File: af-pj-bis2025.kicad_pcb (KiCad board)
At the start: 2 copper layers, 70 x 88.8 mm, 81 parts, among them J1 CN7, J2 CN10, J3 Conn_01x06, J4 Conn_Coaxial, J5 Barrel_Jack_MountingPin, J7 Conn_Coaxial, J8 Conn_01x10, U1 MIC5237-5.0YU, U2 ALD114904APAL, U3 OPA2380AIDGKR, U4 THS4552IPWR, U5 REF5050IDR, U6 LT1991ACMS-TRPBF, U7 UA78L06ACPK, U8 ADS1220IPW

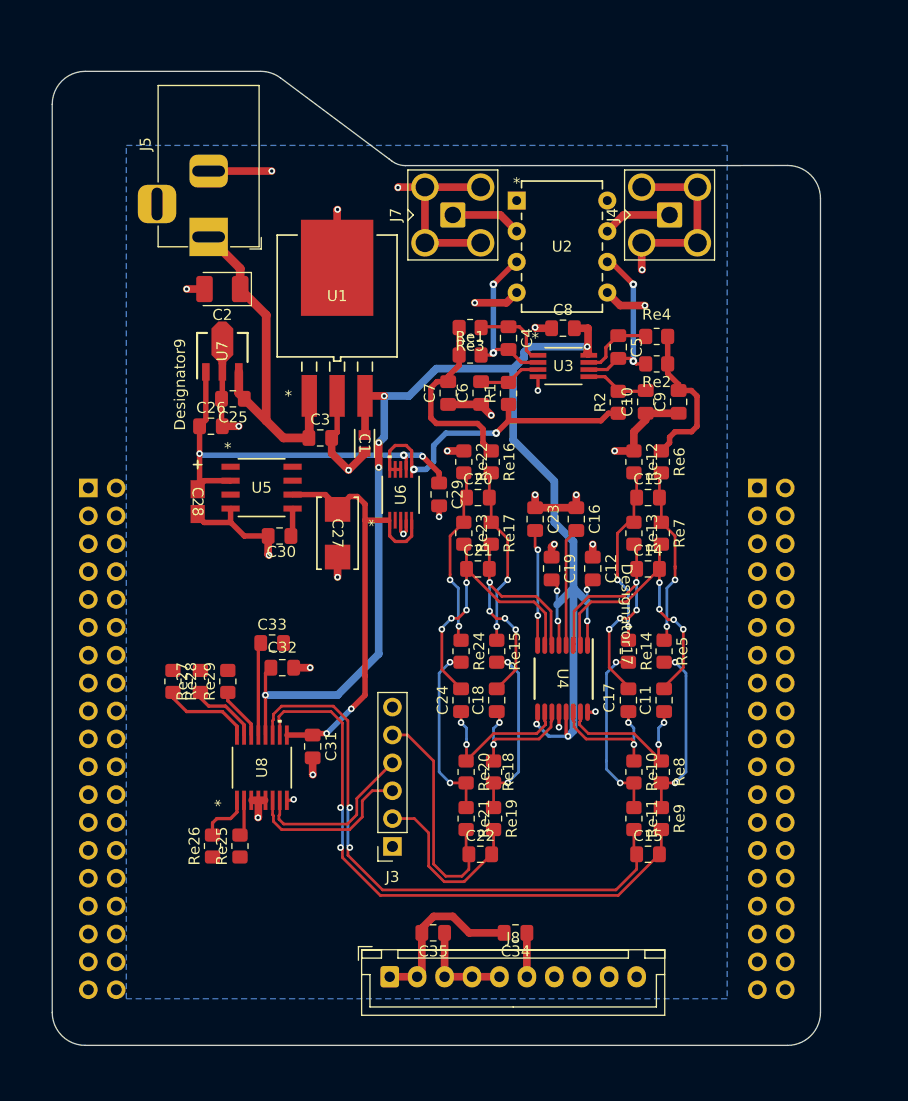
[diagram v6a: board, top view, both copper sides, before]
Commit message: DRC,LVSクリアとテストピン、デバック用ピン追加
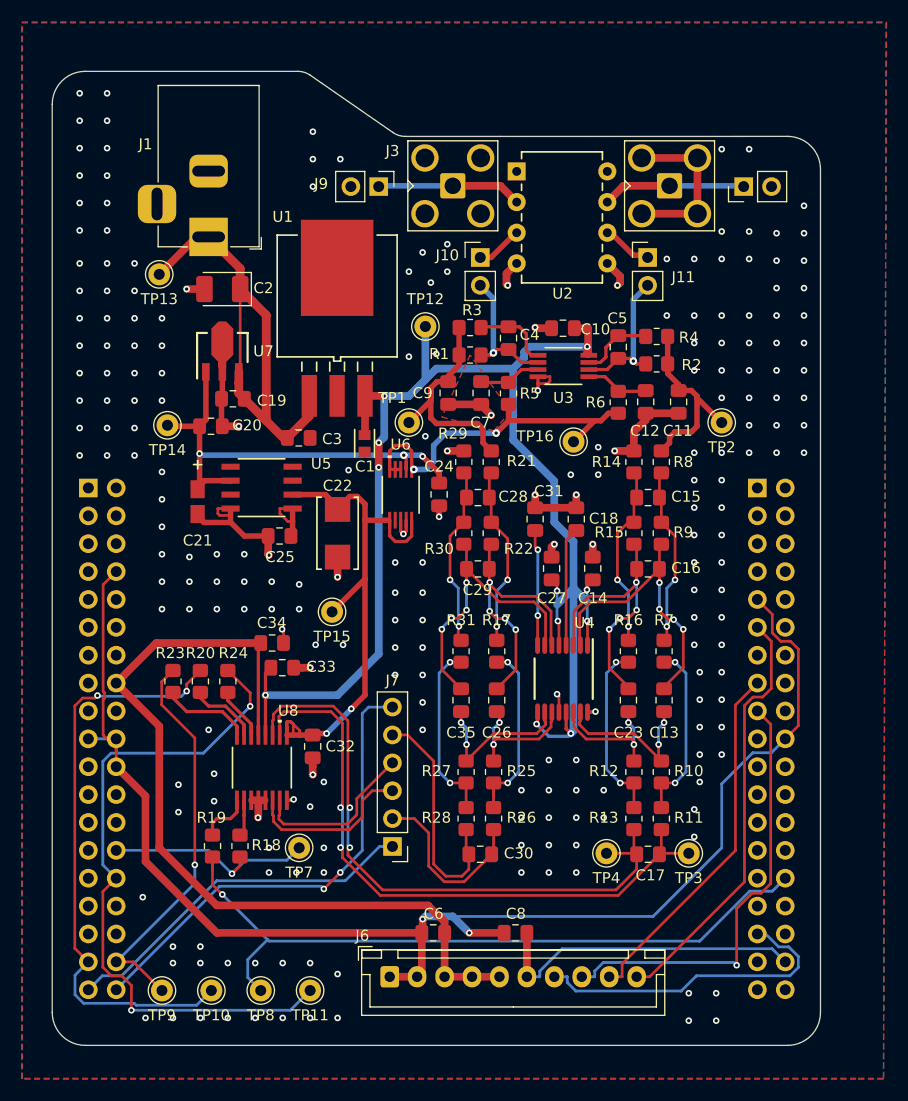
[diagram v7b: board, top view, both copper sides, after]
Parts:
- removed the J1 at (149.8, 88.2)
- removed the J3 at (177.5, 120.9)
- added J10: Conn_01x02, Connector_PinHeader_2.54mm:PinHeader_1x02_P2.54mm_Vertical, F.Cu at (185.5, 67.2)
- added J11: Conn_01x02, Connector_PinHeader_2.54mm:PinHeader_1x02_P2.54mm_Vertical, F.Cu at (200.8, 67.2)
- added J5: CN10, Connector_PinSocket_2.54mm:PinSocket_2x19_P2.54mm_Vertical, B.Cu at (210.8, 88.2)
- added J7: Conn_01x06, Connector_PinHeader_2.54mm:PinHeader_1x06_P2.54mm_Vertical, F.Cu at (177.5, 120.9)
- added J8: Conn_01x02, Connector_PinHeader_2.54mm:PinHeader_1x02_P2.54mm_Vertical, F.Cu at (209.5, 60.8)
- added J9: Conn_01x02, Connector_PinHeader_2.54mm:PinHeader_1x02_P2.54mm_Vertical, F.Cu at (176.2, 60.8)
- added TP1: TestPoint, Connector_Pin:Pin_D1.0mm_L10.0mm, F.Cu at (179.0, 82.2)
- added TP10: TestPoint, Connector_Pin:Pin_D1.0mm_L10.0mm, F.Cu at (161.0, 134.0)
- added TP11: TestPoint, Connector_Pin:Pin_D1.0mm_L10.0mm, F.Cu at (170.0, 134.0)
- added TP12: TestPoint, Connector_Pin:Pin_D1.0mm_L10.0mm, F.Cu at (180.5, 73.5)
- added TP13: TestPoint, Connector_Pin:Pin_D1.0mm_L10.0mm, F.Cu at (156.2, 68.8)
- added TP14: TestPoint, Connector_Pin:Pin_D1.0mm_L10.0mm, F.Cu at (157.0, 82.5)
- added TP15: TestPoint, Connector_Pin:Pin_D1.0mm_L10.0mm, F.Cu at (172.0, 99.5)
- added TP16: TestPoint, Connector_Pin:Pin_D1.0mm_L10.0mm, F.Cu at (194.0, 84.0)
- added TP2: TestPoint, Connector_Pin:Pin_D1.0mm_L10.0mm, F.Cu at (207.5, 82.2)
- added TP3: TestPoint, Connector_Pin:Pin_D1.0mm_L10.0mm, F.Cu at (204.5, 121.5)
- added TP4: TestPoint, Connector_Pin:Pin_D1.0mm_L10.0mm, F.Cu at (197.0, 121.5)
- added TP7: TestPoint, Connector_Pin:Pin_D1.0mm_L10.0mm, F.Cu at (169.0, 121.0)
- added TP8: TestPoint, Connector_Pin:Pin_D1.0mm_L10.0mm, F.Cu at (165.5, 134.0)
- added TP9: TestPoint, Connector_Pin:Pin_D1.0mm_L10.0mm, F.Cu at (156.5, 134.0)
- J2: value CN10 -> CN7
- moved J2 61.0 mm to (149.8, 88.2)
- moved J3 2.66 mm to (183.0, 60.7)
- moved J4 2.66 mm to (202.8, 60.7)
- moved U2 2.66 mm to (188.8, 59.4)
- moved C3 1.96 mm to (169.0, 83.7)
- renumbered C8 to C10, C9 to C11, C10 to C12, C11 to C13, C12 to C14, C13 to C15, C14 to C16, C15 to C17, C16 to C18, C25 to C19, C26 to C20, C28 to C21, C27 to C22, C17 to C23, C29 to C24, C30 to C25, C18 to C26, C19 to C27, C20 to C28, C21 to C29, C22 to C30, C23 to C31, C31 to C32, C32 to C33, C33 to C34, C24 to C35, C35 to C6, C6 to C7, C34 to C8, C7 to C9, J5 to J1, J7 to J3, J8 to J6, Re1 to R1, Re8 to R10, Re9 to R11, Re10 to R12, Re11 to R13, Re12 to R14, Re13 to R15, Re14 to R16, Re15 to R17, Re25 to R18, Re26 to R19, Re2 to R2, Re27 to R20, Re16 to R21, Re17 to R22, Re28 to R23, Re29 to R24, Re18 to R25, Re19 to R26, Re20 to R27, Re21 to R28, Re22 to R29, Re3 to R3, Re23 to R30, Re24 to R31, Re4 to R4, R1 to R5, R2 to R6, Re5 to R7, Re6 to R8, Re7 to R9
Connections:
- C4 pad 2: Net-(U2-DN1) -> Net-(J10-Pin_2)
- C5 pad 2: Net-(U2-DN2) -> Net-(J11-Pin_2)
- J1 pad 3: (no net) -> /AVSS
- J2 pad 12: unconnected-(J2-Pin_12-Pad12) -> /IOREF
- J2 pad 14: unconnected-(J2-Pin_14-Pad14) -> /~{RST}
- J2 pad 16: unconnected-(J2-Pin_16-Pad16) -> +3V3
- J2 pad 18: unconnected-(J2-Pin_18-Pad18) -> +5V
- J2 pad 19: unconnected-(J2-Pin_19-Pad19) -> GND
- J2 pad 22: unconnected-(J2-Pin_22-Pad22) -> GND
- J2 pad 24: unconnected-(J2-Pin_24-Pad24) -> /VIN
- J2 pad 28: unconnected-(J2-Pin_28-Pad28) -> /ADC_CS
- J2 pad 30: unconnected-(J2-Pin_30-Pad30) -> /ADC_DRDY
- J2 pad 32: GNDA -> unconnected-(J2-Pin_32-Pad32)
- J2 pad 33: unconnected-(J2-Pin_33-Pad33) -> +BATT
- J2 pad 35: unconnected-(J2-Pin_35-Pad35) -> /ADC_MISO
- J2 pad 36: unconnected-(J2-Pin_36-Pad36) -> /ADC_MOSI
- J2 pad 37: unconnected-(J2-Pin_37-Pad37) -> /AIN2_mcuN
- J2 pad 38: unconnected-(J2-Pin_38-Pad38) -> /AIN2_mcuP
- J2 pad 5: unconnected-(J2-Pin_5-Pad5) -> VDD
- J2 pad 6: unconnected-(J2-Pin_6-Pad6) -> /E5V
- J2 pad 8: /5V_USB_CHGR -> GND
- J6 pad 7: /LCD_EXCOMIN -> /LCD_EXTCOMIN
- R1 pad 2: Net-(U2-DN1) -> Net-(J10-Pin_2)
- R2 pad 2: Net-(U2-DN2) -> Net-(J11-Pin_2)
- U2 pad 3: Net-(U2-DN1) -> Net-(J10-Pin_1)
- U2 pad 6: Net-(U2-DN2) -> Net-(J11-Pin_1)
- U3 pad 2: Net-(U2-DN1) -> Net-(J10-Pin_2)
- U3 pad 6: Net-(U2-DN2) -> Net-(J11-Pin_2)
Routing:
- net GND: track 15.7 -> 132.5 mm, vias 0 -> 2
- net /ADC_SCLK: track 0.00 -> 66.3 mm, vias 0 -> 1
- net +3V3: track 17.5 -> 83.6 mm
- net /ADC_DRDY: track 0.00 -> 62.0 mm, vias 0 -> 2
- net /ADC_MISO: track 0.00 -> 53.9 mm, vias 0 -> 2
- net /AIN2_mcuP: track 0.00 -> 43.5 mm, vias 0 -> 2
- net /LCD_CS: track 0.00 -> 40.5 mm, vias 0 -> 1
- net /LCD_SCLK: track 0.00 -> 38.7 mm
- net /ADC_MOSI: track 0.00 -> 36.4 mm, vias 0 -> 1
- net /AVSS: track 123.6 -> 89.6 mm, vias 28 -> 231
- net /AIN2_mcuN: track 0.00 -> 33.7 mm
- net /LCD_MOSI: track 0.00 -> 33.0 mm
- net /LCD_EXTCOMIN: track 0.00 -> 29.5 mm
- net /LCD_DISP: track 4.00 -> 29.4 mm
- net /ADC_CS: track 0.00 -> 20.5 mm, vias 0 -> 1
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- added copper zone on F.Cu, net /AVSS
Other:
- outline, holes or cut-outs redrawn

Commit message: 回路が完成した
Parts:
- added G***: LOGO, pj-bis2025:senserity_logo, F.Cu at (210.0, 72.0)
- added TP5: TestPoint, Connector_Pin:Pin_D1.0mm_L10.0mm, F.Cu at (151.5, 82.5)
- renumbered TP8 to TP10, TP9 to TP8, TP10 to TP9
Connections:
- C1 pad 2: /AVSS -> GNDA
- C10 pad 1: /AVSS -> GNDA
- C11 pad 1: /AVSS -> GNDA
- C12 pad 1: /AVSS -> GNDA
- C14 pad 1: /AVSS -> GNDA
- C18 pad 1: /AVSS -> GNDA
- C19 pad 2: /AVSS -> GNDA
- C2 pad 2: /AVSS -> GNDA
- C20 pad 2: /AVSS -> GNDA
- C21 pad 2: /AVSS -> GNDA
- C22 pad 2: /AVSS -> GNDA
- C24 pad 2: /AVSS -> GNDA
- C25 pad 2: /AVSS -> GNDA
- C27 pad 1: /AVSS -> GNDA
- C3 pad 2: /AVSS -> GNDA
- C31 pad 1: /AVSS -> GNDA
- C32 pad 2: /AVSS -> GNDA
- C33 pad 2: /AVSS -> GNDA
- C34 pad 2: /AVSS -> GND
- C7 pad 1: /AVSS -> GNDA
- C9 pad 1: /AVSS -> GNDA
- J1 pad 2: /AVSS -> GNDA
- J1 pad 3: /AVSS -> GNDA
- J3 pad 2: /AVSS -> GNDA
- J4 pad 2: /AVSS -> GNDA
- J8 pad 2: /AVSS -> GNDA
- J9 pad 2: /AVSS -> GNDA
- R14 pad 1: /AVSS -> GNDA
- R29 pad 1: /AVSS -> GNDA
- U1 pad 2: /AVSS -> GNDA
- U1 pad 4: /AVSS -> GNDA
- U2 pad 4: /AVSS -> GNDA
- U2 pad 5: /AVSS -> GNDA
- U3 pad 4: /AVSS -> GNDA
- U4 pad 12: /AVSS -> GNDA
- U4 pad 16: /AVSS -> GNDA
- U5 pad 4: /AVSS -> GNDA
- U6 pad 3: /AVSS -> GNDA
- U6 pad 4: /AVSS -> GNDA
- U7 pad 2: /AVSS -> GNDA
- U8 pad 3: /AVSS -> GNDA
- U8 pad 4: /AVSS -> GND
- U8 pad 5: /AVSS -> GNDA
- U8 pad 8: /AVSS -> GNDA
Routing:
- net /AVSS: track 89.6 -> 0.00 mm, vias 231 -> 0
- net GNDA: track 0.00 -> 89.5 mm, vias 0 -> 239
- net GND: track 132.5 -> 167.2 mm, vias 2 -> 3
- net /DC_9V: track 49.5 -> 41.1 mm
- net /AVDD_5V: track 136.3 -> 138.2 mm
- added copper zone on B.Cu, net GNDA
- added copper zone on F.Cu, net GNDA
- removed copper zone on B.Cu, net /AVSS
- removed copper zone on F.Cu, net /AVSS
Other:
- board text added: "2025 Yusuke Akagi"
